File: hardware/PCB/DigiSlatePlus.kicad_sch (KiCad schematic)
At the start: 18 parts, among them J1 Serial, J2 USB_B, SW1 RotaryEncoder-SW, U1 ESP32-S3-WROOM-1, U2 DS3231M

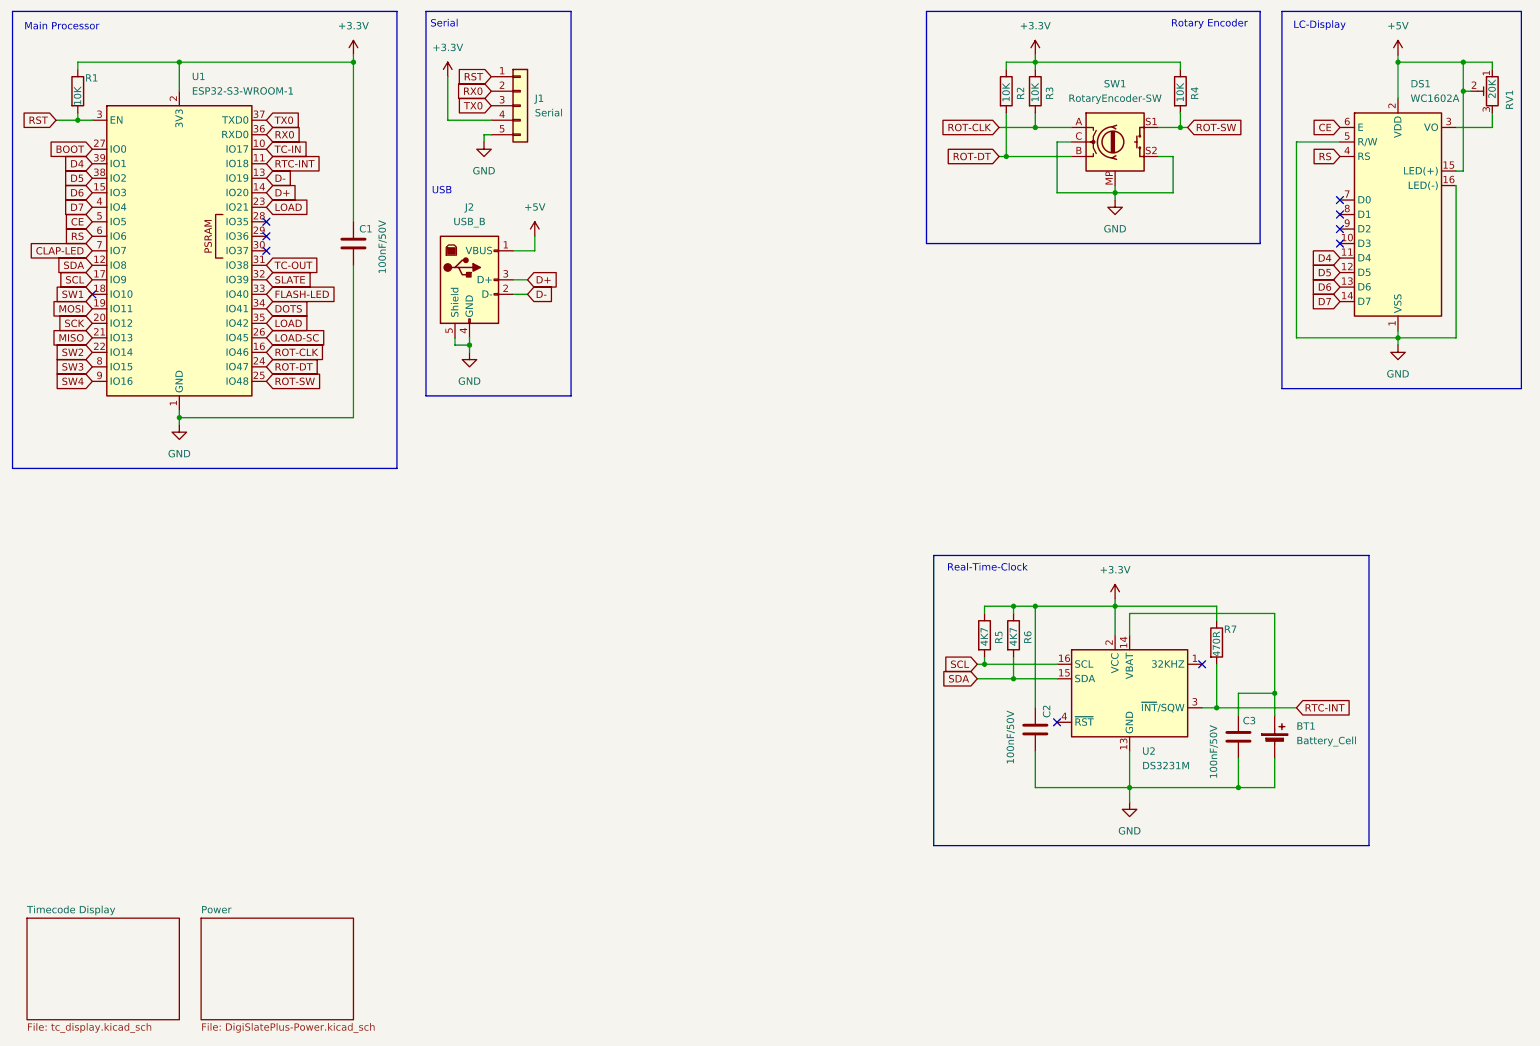
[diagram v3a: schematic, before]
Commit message: schematic and board layout finished
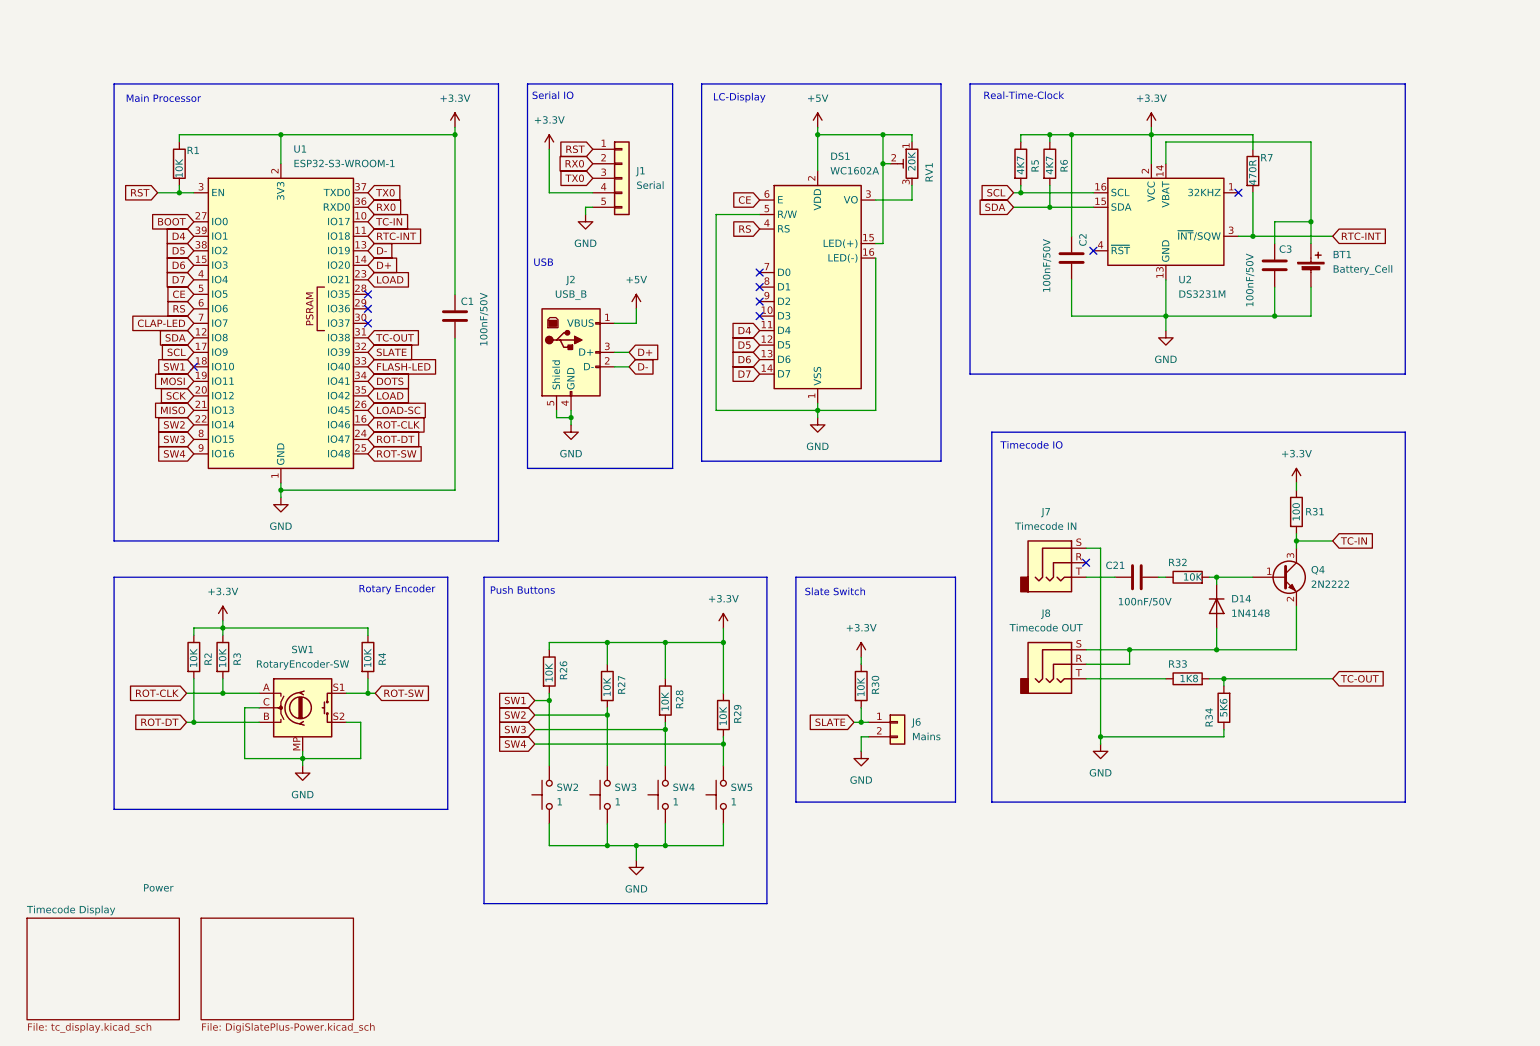
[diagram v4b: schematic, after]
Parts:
- added C21: 100nF/50V, Capacitor_SMD:C_1206_3216Metric_Pad1.33x1.80mm_HandSolder, symbol Device:C
- added D14: 1N4148, Diode_SMD:D_PowerDI-123, symbol Diode:1N4148
- added J6: Mains, Connector_JST:JST_XH_B2B-XH-AM_1x02_P2.50mm_Vertical, symbol Connector_Generic:Conn_01x02
- added J7: Timecode IN, Connector_Audio:Jack_3.5mm_CUI_SJ1-3525N_Horizontal, symbol Connector_Audio:AudioJack3
- added J8: Timecode OUT, Connector_Audio:Jack_3.5mm_CUI_SJ1-3525N_Horizontal, symbol Connector_Audio:AudioJack3
- added Q4: 2N2222, Package_TO_SOT_SMD:SOT-23, symbol Transistor_BJT:MMBT2222A
- added R26, R27, R28, R29, R30, R32: 10K, Resistor_SMD:R_1206_3216Metric, symbol Device:R
- added R31: 100, Resistor_SMD:R_1206_3216Metric, symbol Device:R
- added R33: 1K8, Resistor_SMD:R_1206_3216Metric, symbol Device:R
- added R34: 5K6, Resistor_SMD:R_1206_3216Metric, symbol Device:R
- added SW2, SW3, SW4, SW5: 1, Button_Switch_THT:SW_PUSH-12mm, symbol Switch:SW_Push
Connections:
- net +3.3V: now also R26.1, R27.1, R28.1, R29.1, R30.1, R31.1
- net GND: now also J6.2 (Pin_2), J7.S, R34.1, SW2.1, SW3.1, SW4.1, SW5.1
- net SLATE: now also J6.1 (Pin_1), R30.2
- net SW1: now also R26.2, SW2.2
- net SW2: now also R27.2, SW3.2
- net SW3: now also R28.2, SW4.2
- net SW4: now also R29.2, SW5.2
- net TC-IN: now also Q4.3 (C), R31.2
- net TC-OUT: now also R33.2, R34.2
- new net: D14.1 (K), Q4.1 (B), R32.2
- new net: D14.2 (A), J8.R, J8.S, Q4.2 (E)
- new net: J8.T, R33.1
- new net: C21.2, R32.1
- new net: C21.1, J7.T
- no-connect marks 10 -> 11
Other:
- note added: "Push Buttons"
- note added: "Serial IO"
- note added: "Slate Switch"
- note added: "Timecode IO"
- note removed: "Serial"
- moved on the sheet: BT1, C1, C2, C3, DS1, J1, J2, R1, R2, R3, R4, R5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
